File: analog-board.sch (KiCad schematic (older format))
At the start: 459 parts, among them J1 AC IN, J2 OUT, J3 CONN_20X2, P2 CONN_01X02, Q1 2N3906, Q10 2N3906, Q11 2N3906, Q12 2N3906, Q13 2N3906, Q14 2N3906, Q15 2N3906, Q16 2N3906, Q17 NPN, Q18 NPN, Q19 J111, Q2 2N3906, Q20 2N3906, Q3 2N3906, Q4 2N3906, Q5 2N3906, Q6 BCM857BS, Q7 2N3906, Q8 2N3906, Q9 2N3906, U1 LM13700, U10 ADR01, U11 DG212B, U12 DG212B, U13 DG408, U14 DG408, U15 TL072-, U16 DG408, U17 DG408, U18 LM13700, U19 LM13700, U2 LM13700, U21 TL072-, U22 TL074-, U23 TL074-, U24 TL074-, U25 TL074-, U26 TL072-, U27 TL074-, U28 TL074-, U29 LM13700, U3 LM13700, U30 LM13700, U31 TL074-, U32 LM13700, U33 TL074-, U34 TL074-, U35 TL074-, U36 74LV573, U38 0 - 10V, U39 TL074-, U4 DG212B, U40 DG419, U41 0 - 10V, U42 10 - 0V, U43 LM7812, U44 LM7912, U45 DG408, U46 7805, U5 TL074-, U6 AD5556, U7 TL072-, U8 TL074-, U9 AD8672

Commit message: routing
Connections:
- wire segments 1553 -> 1275

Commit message: routing S&H and CV traces
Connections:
- net labels removed: OSB MIX CV
- wire segments 1275 -> 1554
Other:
- moved on the sheet: C92, U25C, U25D

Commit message: moved audio jack, about to move DAC dmuxers and S&H components
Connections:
- wire segments 1554 -> 1277

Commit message: moved S&H and DAC demuxers, routed 16 of 32 CVs
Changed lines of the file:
@@
 	0    1    1    0
 $EndComp
-Text GLabel 20000 29650 2    60   Output ~ 0
+Text GLabel 19950 26950 2    60   Output ~ 0
 OSCA FM AMT CV
+Text GLabel 22900 26950 2    60   Output ~ 0
+OSC EG2 AMT CV
+Text GLabel 19950 25150 2    60   Output ~ 0
+OSC LFO AMT CV
+Text GLabel 20000 30500 2    60   Output ~ 0
+PWM A LFO AMT CV
 Text GLabel 20000 28500 2    60   Output ~ 0
-OSC EG2 AMT CV
+OSCA INIT CV
 Text GLabel 19950 24000 2    60   Output ~ 0
-OSC LFO AMT CV
-Text GLabel 19950 26950 2    60   Output ~ 0
-PWM A LFO AMT CV
+PWM A EG2 AMT CV
 Text GLabel 20000 31450 2    60   Output ~ 0
-OSCA INIT CV
-Text GLabel 19950 25150 2    60   Output ~ 0
-PWM A EG2 AMT CV
-Text GLabel 19950 26000 2    60   Output ~ 0
 PWM A CV
+Text GLabel 22900 25150 2    60   Output ~ 0
+GLIDE AMT CV
+Text GLabel 22900 24000 2    60   Output ~ 0
+OSCA PITCH CV
 Text GLabel 22900 26000 2    60   Output ~ 0
-GLIDE AMT CV
-Text GLabel 22900 25150 2    60   Output ~ 0
-OSCA PITCH CV
-Text GLabel 22900 26950 2    60   Output ~ 0
 OSCB PITCH CV
+Text GLabel 22900 31450 2    60   Output ~ 0
+OSCB INIT CV
 Text GLabel 22900 30500 2    60   Output ~ 0
-OSCB INIT CV
-Text GLabel 22900 24000 2    60   Output ~ 0
 PWM B CV
 $Comp
@@
 Text Notes 36900 15350 0    60   ~ 0
 Adjust R(Iabc) for unity gain
-Text GLabel 22900 31450 2    60   Output ~ 0
+Text GLabel 22900 29650 2    60   Output ~ 0
 OSCA MIX CV
-Text GLabel 20000 30500 2    60   Output ~ 0
+Text GLabel 20000 29650 2    60   Output ~ 0
 NOISE MIX CV
-Text GLabel 22900 29650 2    60   Output ~ 0
+Text GLabel 22900 28500 2    60   Output ~ 0
 OSCB MIX CV
 Text GLabel 25700 28500 2    60   Output ~ 0
@@
 Text GLabel 25700 25150 2    60   Output ~ 0
 RES CV
-Text GLabel 22900 28500 2    60   Output ~ 0
+Text GLabel 25700 26950 2    60   Output ~ 0
 VOL CV
-Text GLabel 25700 26950 2    60   Output ~ 0
+Text GLabel 19950 26000 2    60   Output ~ 0
 LFO RATE CV
 Text GLabel 28350 23950 2    60   Output ~ 0

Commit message: routing
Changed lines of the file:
@@
 Text GLabel 24350 25250 0    60   Input ~ 0
 SH17
-Text GLabel 24350 27050 0    60   Input ~ 0
+Text GLabel 24350 26100 0    60   Input ~ 0
 SH19
 Text GLabel 24350 28600 0    60   Input ~ 0
@@
 Text GLabel 24350 29750 0    60   Input ~ 0
 SH21
-Text GLabel 24350 26100 0    60   Input ~ 0
+Text GLabel 24350 27050 0    60   Input ~ 0
 SH18
 Text GLabel 24350 30600 0    60   Input ~ 0
@@
 Text GLabel 22900 28500 2    60   Output ~ 0
 OSCB MIX CV
-Text GLabel 25700 28500 2    60   Output ~ 0
+Text GLabel 25700 26000 2    60   Output ~ 0
 KEYTRACK AMT CV
-Text GLabel 25700 30500 2    60   Output ~ 0
+Text GLabel 25700 26950 2    60   Output ~ 0
 FIL EG2 AMT CV
-Text GLabel 25700 24000 2    60   Output ~ 0
+Text GLabel 25700 28500 2    60   Output ~ 0
 CUTOFF CV
-Text GLabel 25700 29650 2    60   Output ~ 0
+Text GLabel 25700 25150 2    60   Output ~ 0
 FIL LFO AMT CV
-Text GLabel 25700 31450 2    60   Output ~ 0
+Text GLabel 25700 24000 2    60   Output ~ 0
 FIL OSCB  AMT CV
-Text GLabel 25700 26000 2    60   Output ~ 0
+Text GLabel 25700 30500 2    60   Output ~ 0
 AMP LFO AMT CV
-Text GLabel 25700 25150 2    60   Output ~ 0
+Text GLabel 25700 29650 2    60   Output ~ 0
 RES CV
-Text GLabel 25700 26950 2    60   Output ~ 0
+Text GLabel 25700 31450 2    60   Output ~ 0
 VOL CV
 Text GLabel 19950 26000 2    60   Output ~ 0

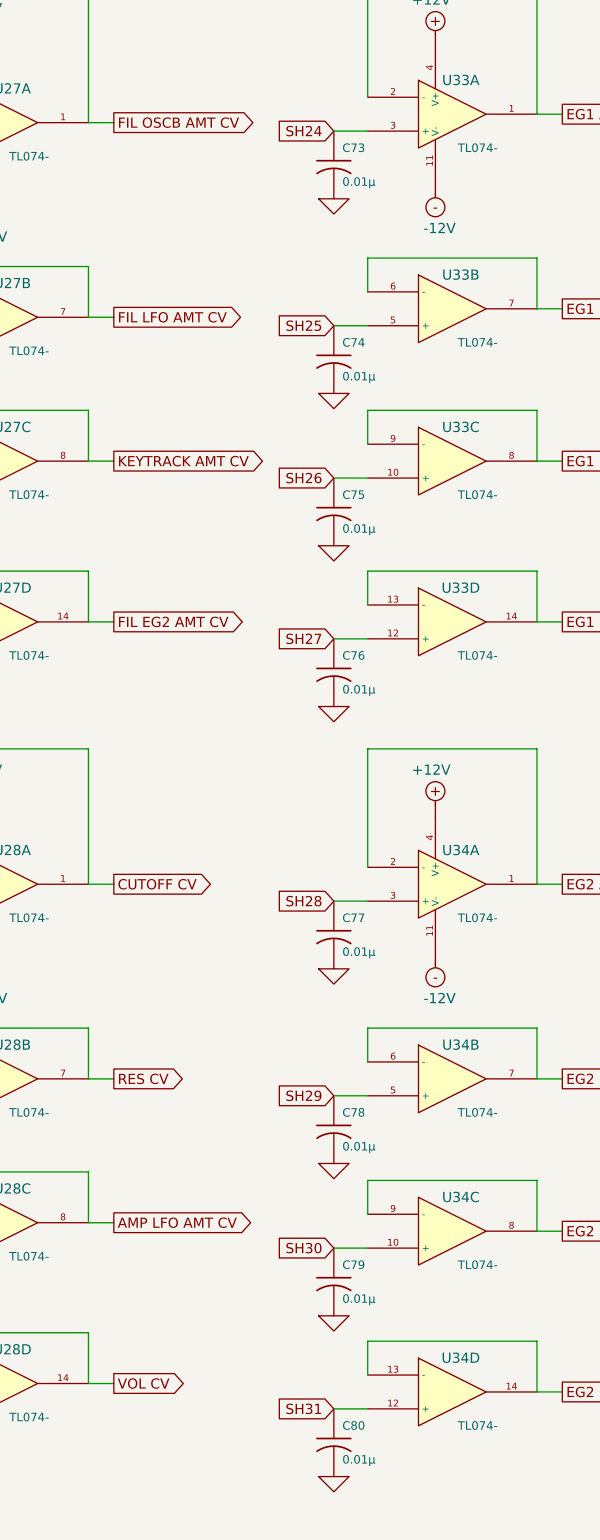
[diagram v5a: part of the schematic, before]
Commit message: component placement done. need to add more bypass caps and route power traces
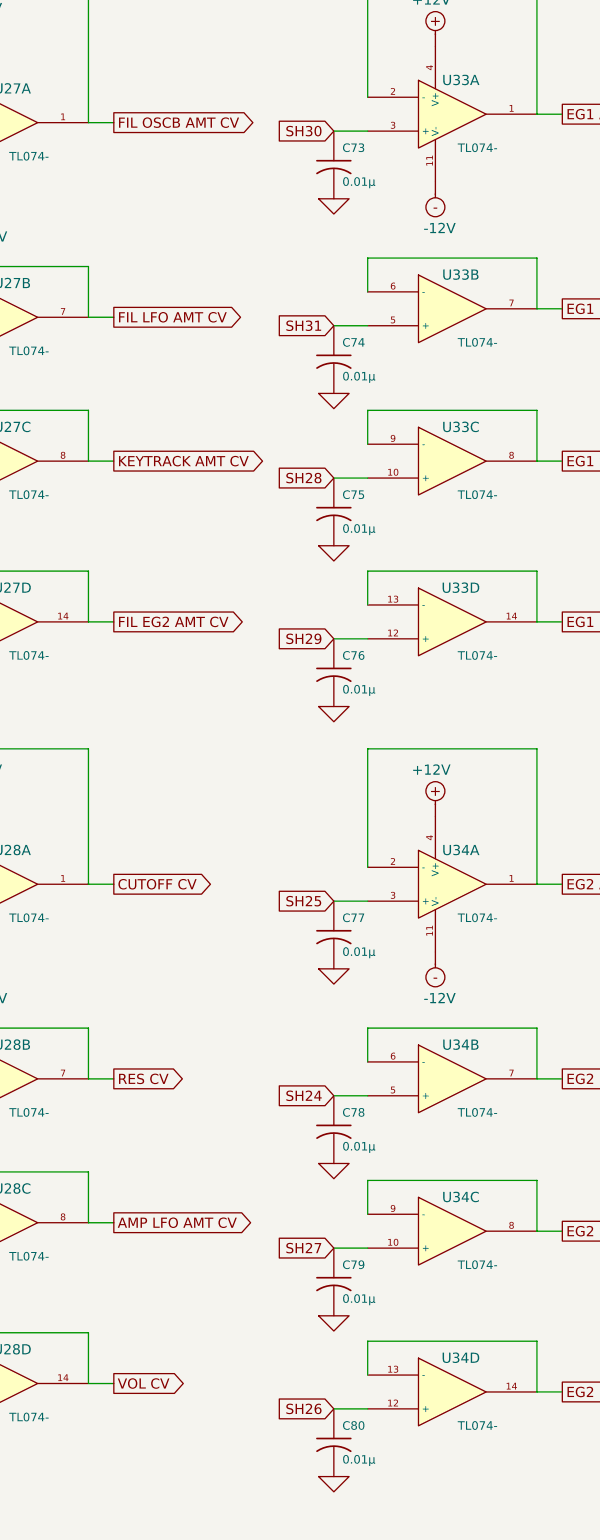
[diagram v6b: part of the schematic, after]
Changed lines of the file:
@@
 	1    0    0    -1
 $EndComp
-Text GLabel 27000 25200 0    60   Input ~ 0
+Text GLabel 27000 28600 0    60   Input ~ 0
 SH25
-Text GLabel 27000 24050 0    60   Input ~ 0
+Text GLabel 27000 29750 0    60   Input ~ 0
 SH24
 $Comp
@@
 	1    0    0    -1
 $EndComp
-Text GLabel 27000 26100 0    60   Input ~ 0
+Text GLabel 27000 31600 0    60   Input ~ 0
 SH26
 $Comp
@@
 	1    0    0    -1
 $EndComp
-Text GLabel 27000 27050 0    60   Input ~ 0
+Text GLabel 27000 30650 0    60   Input ~ 0
 SH27
 $Comp
@@
 Text GLabel 16850 31200 2    40   Output ~ 0
 SH31
-Text GLabel 27000 29750 0    60   Input ~ 0
+Text GLabel 27000 27050 0    60   Input ~ 0
 SH29
-Text GLabel 27000 28600 0    60   Input ~ 0
+Text GLabel 27000 26100 0    60   Input ~ 0
 SH28
 $Comp
@@
 	1    0    0    -1
 $EndComp
-Text GLabel 27000 30650 0    60   Input ~ 0
+Text GLabel 27000 24050 0    60   Input ~ 0
 SH30
 $Comp
@@
 	1    0    0    -1
 $EndComp
-Text GLabel 27000 31600 0    60   Input ~ 0
+Text GLabel 27000 25200 0    60   Input ~ 0
 SH31
 $Comp

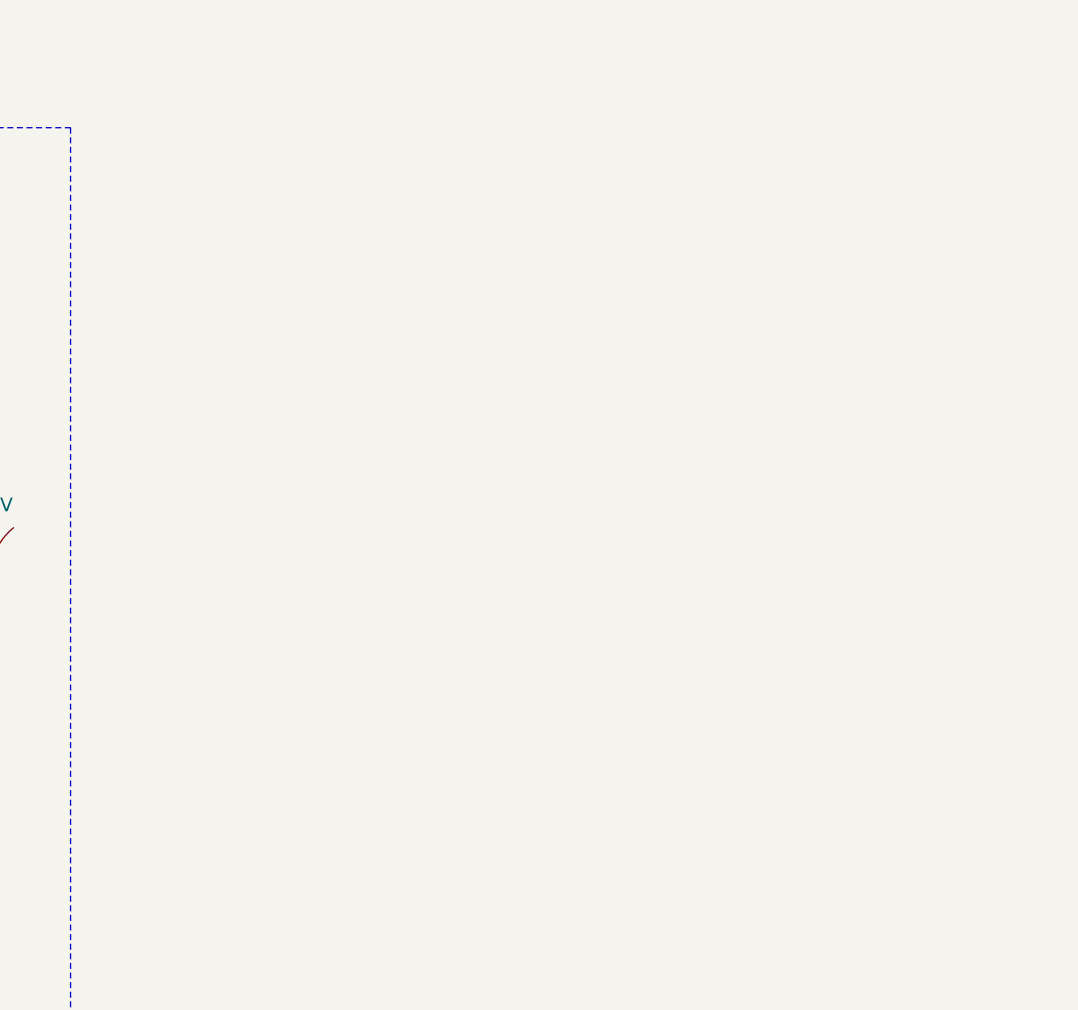
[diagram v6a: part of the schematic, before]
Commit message: added decoupling caps for op amps, need one more pair. started routing power. Oh boy...
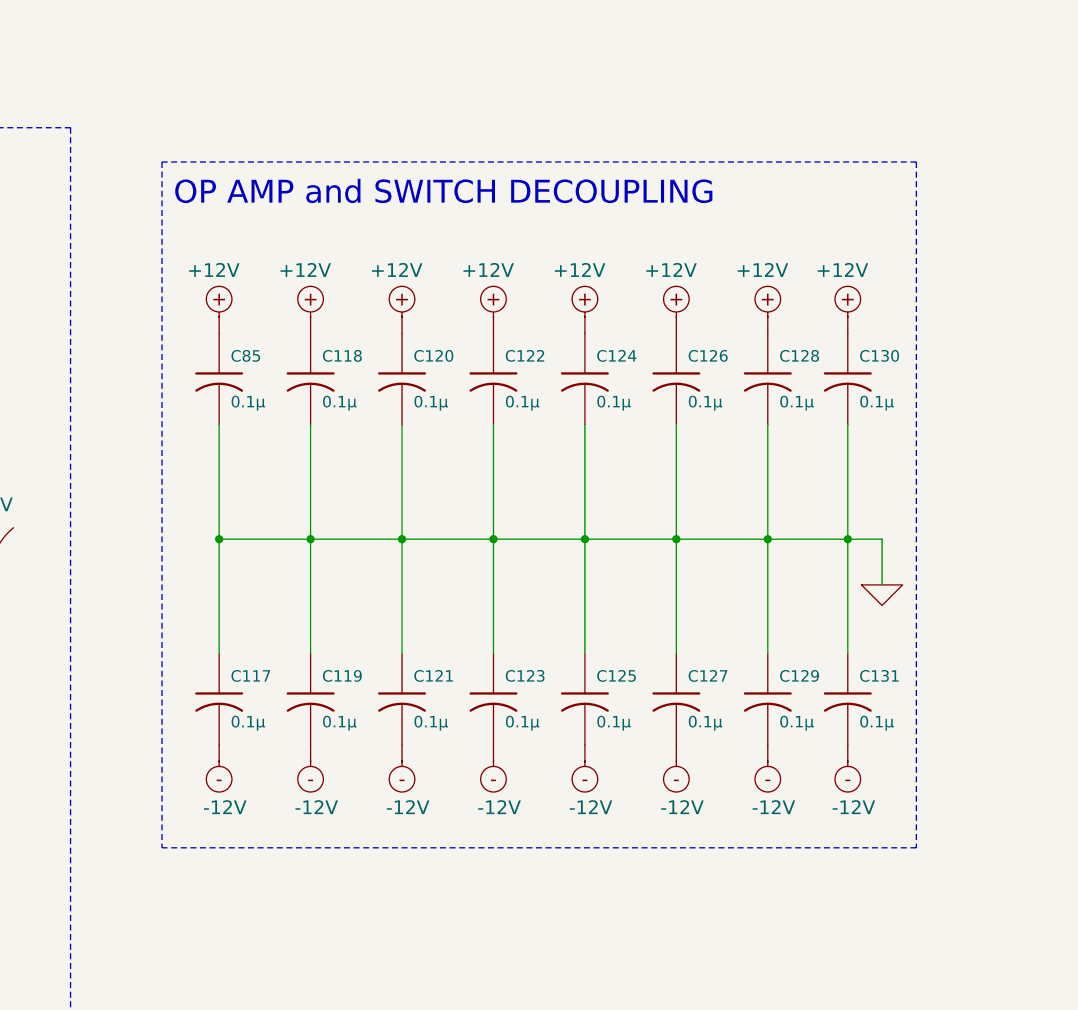
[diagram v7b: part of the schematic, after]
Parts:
- added C117, C118, C119, C120, C121, C122, C123, C124, C125, C126, C127, C128, C129, C130, C131, C85: 0.1µ, ~, symbol C_US
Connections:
- wire segments 1277 -> 1287
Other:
- note added: "OP AMP and SWITCH DECOUPLING"

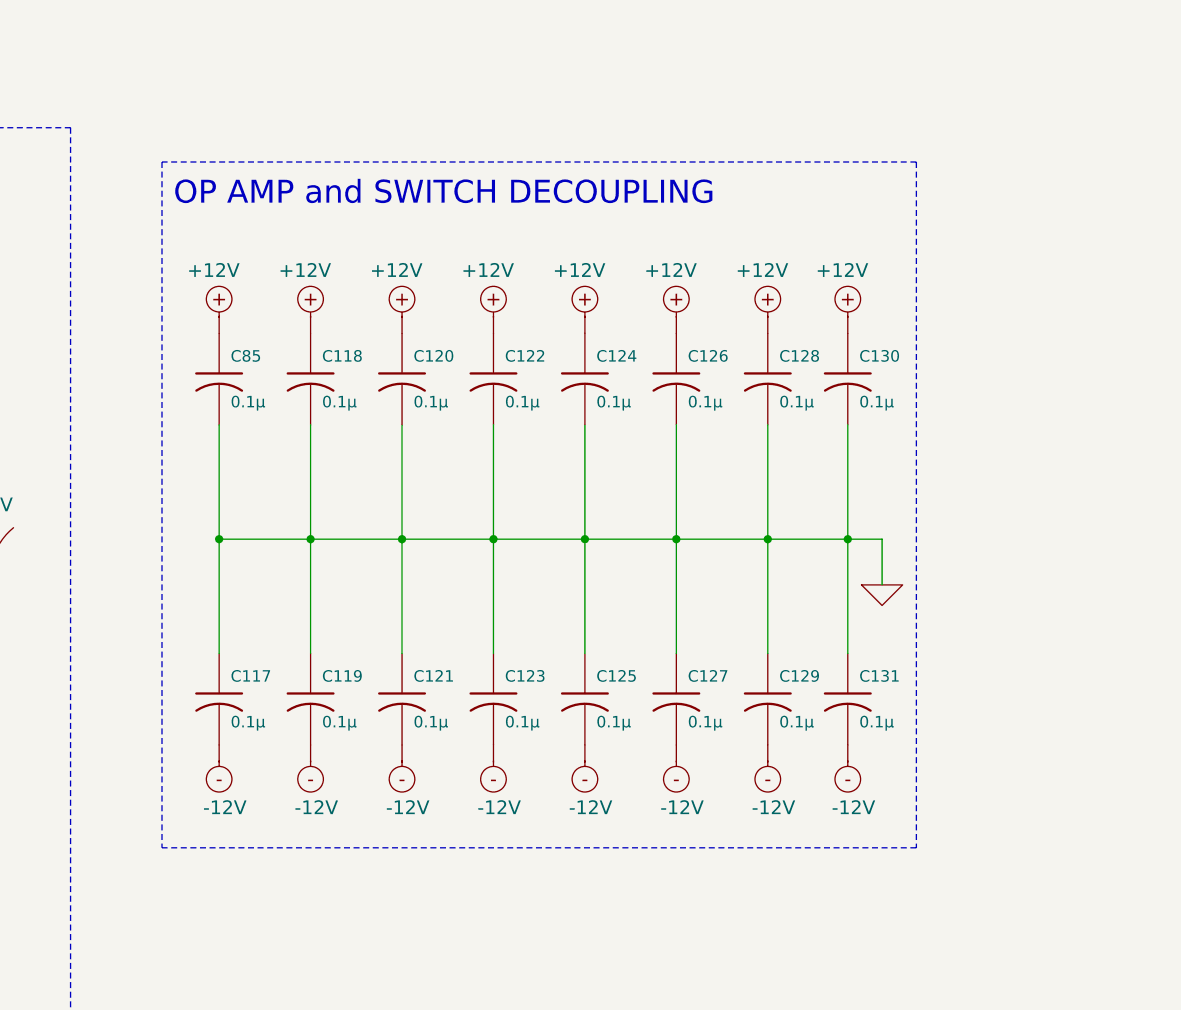
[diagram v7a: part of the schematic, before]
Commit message: almost done routing pos and neg 12V power traces, but 5V traces are provign difficult. Going to branch now and start over again routing power traces first
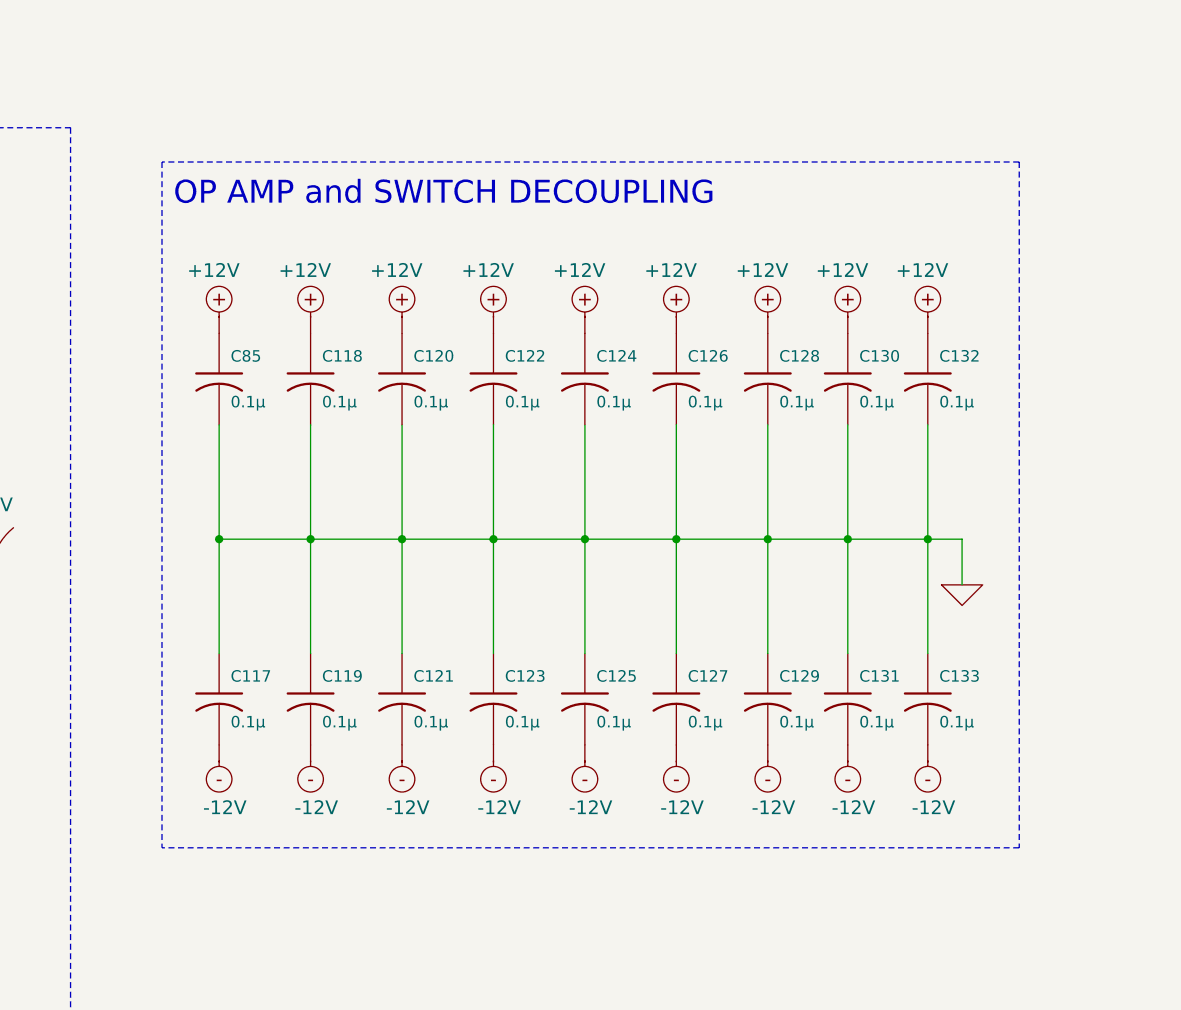
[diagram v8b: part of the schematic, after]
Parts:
- added C132, C133: 0.1µ, ~, symbol C_US
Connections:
- wire segments 1287 -> 1288
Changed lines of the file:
@@
 L +12V #PWR0321
 U 1 1 54F91C16
-P 40800 28500
-F 0 "#PWR0321" H 40800 28600 30  0001 C CNN
-F 1 "+12V" H 40775 28775 60  0000 C CNN
-F 2 "~" H 40800 28500 60  0000 C CNN
-F 3 "~" H 40800 28500 60  0000 C CNN
-	1    40800 28500
+P 41150 28500
+F 0 "#PWR0321" H 41150 28600 30  0001 C CNN
+F 1 "+12V" H 41125 28775 60  0000 C CNN
+F 2 "~" H 41150 28500 60  0000 C CNN
+F 3 "~" H 41150 28500 60  0000 C CNN
+	1    41150 28500
 	1    0    0    -1
 $EndComp
@@
 L -12V #PWR0327
 U 1 1 54F91C5F
-P 40800 30300
-F 0 "#PWR0327" H 40800 30400 30  0001 C CNN
-F 1 "-12V" H 40775 30575 60  0000 C CNN
-F 2 "~" H 40800 30300 60  0000 C CNN
-F 3 "~" H 40800 30300 60  0000 C CNN
-	1    40800 30300
+P 41150 30300
+F 0 "#PWR0327" H 41150 30400 30  0001 C CNN
+F 1 "-12V" H 41125 30575 60  0000 C CNN
+F 2 "~" H 41150 30300 60  0000 C CNN
+F 3 "~" H 41150 30300 60  0000 C CNN
+	1    41150 30300
 	-1   0    0    1
 $EndComp
@@
 L GND #PWR0330
 U 1 1 54F91C7D
-P 40950 29600
-F 0 "#PWR0330" H 40950 29600 30  0001 C CNN
-F 1 "GND" H 40950 29530 30  0001 C CNN
-F 2 "~" H 40950 29600 60  0000 C CNN
-F 3 "~" H 40950 29600 60  0000 C CNN
-	1    40950 29600
+P 41300 29600
+F 0 "#PWR0330" H 41300 29600 30  0001 C CNN
+F 1 "GND" H 41300 29530 30  0001 C CNN
+F 2 "~" H 41300 29600 60  0000 C CNN
+F 3 "~" H 41300 29600 60  0000 C CNN
+	1    41300 29600
 	1    0    0    -1
 $EndComp
@@
 	37800 27750 37800 30750
 Wire Notes Line
-	41100 27750 41100 30750
+	41550 27750 41550 30750
 Wire Notes Line
-	41100 27750 37800 27750
+	41550 27750 37800 27750
 Wire Notes Line
-	41100 30750 37800 30750
+	41550 30750 37800 30750
 Wire Wire Line
 	38850 28900 38850 29900
@@
 	40450 28900 40450 29900
 Wire Wire Line
-	40800 28900 40800 29900
-Wire Wire Line
-	40950 29400 40950 29600
-Wire Wire Line
-	38050 29400 40950 29400
-Connection ~ 40800 29400
+	41150 28900 41150 29900
+Wire Wire Line
+	41300 29400 41300 29600
+Wire Wire Line
+	38050 29400 41300 29400
+Connection ~ 41150 29400
 Connection ~ 40450 29400
 Connection ~ 40050 29400
@@
 Connection ~ 38450 29400
 Connection ~ 38050 29400
+$Comp
+L C_US C132
+U 1 1 54FA3AB0
+P 41150 28700
+F 0 "C132" H 41200 28800 50  0000 L CNN
+F 1 "0.1µ" H 41200 28600 50  0000 L CNN
+F 2 "~" H 41150 28700 60  0000 C CNN
+F 3 "~" H 41150 28700 60  0000 C CNN
+	1    41150 28700
+	1    0    0    -1
+$EndComp
+$Comp
+L +12V #PWR0335
+U 1 1 54FA3AB6
+P 40800 28500
+F 0 "#PWR0335" H 40800 28600 30  0001 C CNN
+F 1 "+12V" H 40775 28775 60  0000 C CNN
+F 2 "~" H 40800 28500 60  0000 C CNN
+F 3 "~" H 40800 28500 60  0000 C CNN
+	1    40800 28500
+	1    0    0    -1
+$EndComp
+Wire Wire Line
+	40800 28900 40800 29900
+$Comp
+L C_US C133
+U 1 1 54FA3F34
+P 41150 30100
+F 0 "C133" H 41200 30200 50  0000 L CNN
+F 1 "0.1µ" H 41200 30000 50  0000 L CNN
+F 2 "~" H 41150 30100 60  0000 C CNN
+F 3 "~" H 41150 30100 60  0000 C CNN
+	1    41150 30100
+	1    0    0    -1
+$EndComp
+$Comp
+L -12V #PWR0336
+U 1 1 54FA3F3A
+P 40800 30300
+F 0 "#PWR0336" H 40800 30400 30  0001 C CNN
+F 1 "-12V" H 40775 30575 60  0000 C CNN
+F 2 "~" H 40800 30300 60  0000 C CNN
+F 3 "~" H 40800 30300 60  0000 C CNN
+	1    40800 30300
+	-1   0    0    1
+$EndComp
+Connection ~ 40800 29400
 $EndSCHEMATC
